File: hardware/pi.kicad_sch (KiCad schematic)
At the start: 4 parts, among them U1 RP2040, U2 W25Q128JVSIQ, U3 TJA1042T_3_1J, U4 105450-0101

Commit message: work on pi schematic
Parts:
- added C1, C2: 27p, jlc_footprints:C0402, symbol jlc:C0402C0G270G500NTB
- added C10, C11, C12, C13, C14, C5, C6, C7, C8, C9: 100nF, jlc_footprints:C0402, symbol jlc:CC0402KRX7R8BB104
- added C3, C4: 1uF, jlc_footprints:C0402, symbol jlc:0402X105K160
- added R1, R2: 5K1, jlc_footprints:R0402, symbol jlc:CR-02FL6---5K1
- added R3: 1K, jlc_footprints:R0402, symbol jlc:CR-02FL6----1K
- added R4, R5: 27R4, jlc_footprints:R0402, symbol jlc:WR04X27R4FTL
- added U5: NCP1117ST33T3G, jlc_footprints:SOT-223-3_L6.5-W3.4-P2.30-LS7.0-BR, symbol jlc:NCP1117ST33T3G
- added U6: SS54_C22452, jlc_footprints:SMA_L4.4-W2.8-LS5.4-R-RD, symbol jlc:SS54_C22452
- added U7: DS1129-05-S80BP-X, jlc_footprints:RJ45-TH_DS1129-05-S80BP-X, symbol jlc:DS1129-05-S80BP-X
- added X1: 12MHz, jlc_footprints:OSC-SMD_2P-L5.0-W3.2, symbol jlc:ABM3-12_000MHZ-D2Y-T
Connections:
- net USBC.GND is gone; now on net GND: U4.A1 (GND), U4.A12 (GND), U4.B1 (GND), U4.B12 (GND)
- net USBC.DM: now also R5.2; no longer U1.46 (USB_DM)
- net USBC.DP: now also R4.2; no longer U1.47 (USB_DP)
- net USBC.VBUS: now also U6.1 (A)
- net at U4.A5 (CC1): now also R2.1
- net at U4.B5 (CC2): now also R1.1
- net +3.3V: now reaches U1.1 (IOVDD)
- net +3.3V: now also U1.10 (IOVDD), U1.22 (IOVDD), U1.33 (IOVDD), U1.42 (IOVDD), U1.43 (ADC_AVDD), U1.44 (VREG_IN), U1.48 (USB_VDD), U1.49 (IOVDD), C10.1, C11.1, C12.1, C13.1, C14.1, C4.1, C7.1, C8.1, C9.1
- net GND: now reaches U1.19 (TESTEN)
- net GND: now also U1.57 (GND), C1.1, C10.2, C11.2, C12.2, C13.2, C14.2, C2.1, C3.2, C4.2, C5.2, C6.2, C7.2, C8.2, C9.2, R1.2, R2.2
- net at U1.20 (XIN): now also C1.2, X1.1 (OSC1)
- net at U1.21 (XOUT): now also R3.2
- net +1V1: now reaches U1.23 (DVDD)
- net +1V1: now also U1.45 (VREG_VOUT), U1.50 (DVDD), C3.1, C5.1, C6.1
- new net: R4.1, U1.47 (USB_DP)
- new net: R5.1, U1.46 (USB_DM)
- new net: C2.2, R3.1, X1.2 (OSC2)
- new net +5V: U6.2 (K)
- no-connect marks 0 -> 10
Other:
- title: (none) -> Pi RP2040 MCU
- moved on the sheet: U1, U2, U3, U4

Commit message: continue work on pi part
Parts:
- added C15, C18: 100nF, jlc_footprints:C0402, symbol jlc:CC0402KRX7R8BB104
- added C16, C17: 10uF, jlc_footprints:C0603, symbol jlc:TCC0603X5R106M100CT
- added C19: 4.7nF, jlc_footprints:C0402, symbol jlc:0402B472K500CT
- added C20, C21: 100pF, jlc_footprints:C0402, symbol jlc:CC0402JRNPO9BN101
- added C22: 47nF, jlc_footprints:C0402, symbol jlc:GCM155R71H473KE02J
- added H1: WS2812, jlc_footprints:HDR-TH_3P-P2.54-V-F, symbol jlc:22025403P00CKMT
- added H2: Debug, jlc_footprints:HDR-TH_6P-P2.54-V-F, symbol jlc:Header-Female-2_54_1x6
- added H3: T_CH, jlc_footprints:HDR-TH_2P-P2.54-V-M-1, symbol jlc:22-28-4020
- added H4: T_CL, jlc_footprints:HDR-TH_2P-P2.54-V-M-1, symbol jlc:22-28-4020
- added R10: 1M, jlc_footprints:R0402, symbol jlc:AC0402FR-071ML
- added R11, R12: 60R4, jlc_footprints:R1206, symbol jlc:AC1206FR-0760R4L
- added R6, R9: 1K, jlc_footprints:R0402, symbol jlc:CR-02FL6----1K
- added R7, R8: 10K, jlc_footprints:R0402, symbol jlc:CR-02FL6---10K
- added SW1: BOOTSEL, jlc_footprints:SW-SMD_L6.1-W3.6-LS6.6, symbol jlc:TS-1092U-B3D2
- added SW2: RESET, jlc_footprints:SW-SMD_L6.1-W3.6-LS6.6, symbol jlc:TS-1092U-B3D2
- added U8: WS2812E-V5, jlc_footprints:LED-SMD_4P-L5.0-W5.0-LS5.4-TL-1, symbol jlc:WS2812E-V5
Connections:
- net +3.3V: now also U2.8 (VCC), U3.5 (VIO), U5.2 (OUTPUT), U5.4 (TAB), C15.1, C17.1, C18.2, H2.1, R7.1, R8.2
- net +5V: now also U3.3 (VCC), U5.3 (INPUT), C16.1, C18.1, C22.1, H1.3, U8.1 (VDD)
- net GND: now also U2.4 (GND), U3.2 (GND), U3.8 (STB), U5.1 (ADJ/GND), C15.2, C16.2, C17.2, C19.2, C20.2, C21.1, C22.2, H1.1, H2.2, R10.2, SW1.2, SW2.2, U8.3 (GND)
- net SPI_FLASH.SS: now also R6.2, R7.2
- net at U7.17: now also U7.18, U7.19
- net USBC.SHIELD: now reaches U4.0 (25)
- net USBC.SHIELD: now also R10.1
- net at U3.1 (TXD): now also U1.36 (GPIO24)
- net at U3.4 (RXD): now also U1.37 (GPIO25)
- net at U3.6 (CANL): now also C21.2, H4.2
- net at U3.7 (CANH): now also C20.1, H3.2
- net IO8: now reaches U1.11 (GPIO8)
- net IO9: now reaches U1.12 (GPIO9)
- net IO10: now reaches U1.13 (GPIO10)
- net IO11: now reaches U1.14 (GPIO11)
- net I2C_SDA: now reaches U1.17 (GPIO14)
- net I2C_SCL: now reaches U1.18 (GPIO15)
- net IO0: now reaches U1.2 (GPIO0)
- net Debug_Clock: now reaches U1.24 (SWCLK)
- net Debug_Clock: now also H2.3
- net Debug_Data: now reaches U1.25 (SWD)
- net Debug_Data: now also H2.4
- net at U1.26 (RUN): now also R8.1, R9.1
- net Debug_Tx: now reaches U1.27 (GPIO16)
- net Debug_Tx: now also H2.5
- net Debug_Rx: now reaches U1.28 (GPIO17)
- net Debug_Rx: now also H2.6
- net IO1: now reaches U1.3 (GPIO1)
- net LED_Din: now reaches U1.35 (GPIO23)
- net LED_Din: now also U8.4 (DIN)
- net ADC0: now reaches U1.38 (GPIO26_ADC0)
- net ADC1: now reaches U1.39 (GPIO27_ADC1)
- net IO2: now reaches U1.4 (GPIO2)
- net ADC2: now reaches U1.40 (GPIO28_ADC2)
- net ADC3: now reaches U1.41 (GPIO29_ADC3)
- net IO3: now reaches U1.5 (GPIO3)
- net IO4: now reaches U1.6 (GPIO4)
- net IO5: now reaches U1.7 (GPIO5)
- net IO6: now reaches U1.8 (GPIO6)
- net IO7: now reaches U1.9 (GPIO7)
- new net: C19.1, R11.2, R12.1
- new net: H4.1, R12.2
- new net: H1.2, U8.2 (DO)
- new net: H3.1, R11.1
- new net: R9.2, SW2.1
- new net: R6.1, SW1.1
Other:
- note added: "3.3V Power Supply"
- note added: "CAN Transceiver"
- note added: "Debugging Connector"
- note added: "Status LED"
- moved on the sheet: U2, U3, U5, U7A, U7B

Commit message: more work on pi schematic
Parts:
- added C23: 100nF, jlc_footprints:C0402, symbol jlc:CC0402KRX7R8BB104
- added C24: 100uF, jlc_footprints:CAP-SMD_BD10.0-L10.3-W10.3-FD, symbol jlc:VZH101M1K1010-TRO
- added C25: 1000uF, jlc_footprints:CAP-SMD_BD10.0-L10.3-W10.3-LS11.3-FD, symbol jlc:VT1C102M1010
- added D1: MBR340F, jlc_footprints:SOD-123_L2.8-W1.8-LS3.7-RD, symbol jlc:MBR340F
- added H5: PWR, jlc_footprints:HDR-TH_2P-P2.54-V-M-1, symbol jlc:22-28-4020
- added R13, R14, R15, R16: 10K, jlc_footprints:R0402, symbol jlc:CR-02FL6---10K
- added R17: 1M, jlc_footprints:R0402, symbol jlc:AC0402FR-071ML
- added U10: SKCR-16S, jlc_footprints:SW-SMD_SM_SKCR-16S, symbol jlc:SKCR-16S
- added U11: LM2576S-5_0_TR, jlc_footprints:TO-263-5_L10.6-W9.6-P1.70-LS15.9-BR, symbol jlc:LM2576S-5_0_TR
- added U12: SS54_C22452, jlc_footprints:SMA_L4.4-W2.8-LS5.4-R-RD, symbol jlc:SS54_C22452
- added U13: 100uH, jlc_footprints:IND-SMD_L11.5-W10.0_YSPI1050, symbol jlc:YSPI1050-101M
- added U9: 74HC165D,653, jlc_footprints:SOIC-16_L9.9-W3.9-P1.27-LS6.0-BL, symbol jlc:74HC165D,653
- U7: value DS1129-05-S80BP-X -> CAN_IO
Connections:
- net +3.3V: now also C23.2, R13.1, R14.1, R15.1, R16.1, U9.16 (VCC)
- net +5V: now also U12.2 (K)
- net GND: now also U7.11, U7.14, U7.15, U7.3, U7.6, U7.7, C23.1, C24.2, C25.2, D1.2, R17.2, U10.C1 (C), U10.C2 (C), U11.3 (GND), U11.5 (ON#/OFF), U11.6 (TAB), U9.10 (DS), U9.15 (CE#), U9.8 (GND)
- net at C21.2, H4.2, U3.6 (CANL): now also U7.10, U7.2
- net at U7.1: now also C20.1, H3.2, U3.7 (CANH), U7.9
- net at U7.17, U7.18, U7.19: now also R17.1
- net at U7.4: now also U7.12, U7.13, U7.16, U7.5, U7.8, H5.1
- net IO12: now reaches U1.15 (GPIO12)
- net IO13: now reaches U1.16 (GPIO13)
- net IO14: now reaches U1.29 (GPIO18)
- net IO15: now reaches U1.30 (GPIO19)
- net SR_Load: now reaches U1.31 (GPIO20)
- net SR_Load: now also U9.1 (PL#)
- net SR_Clock: now reaches U1.32 (GPIO21)
- net SR_Clock: now also U9.2 (CP)
- net SR_Data: now reaches U1.34 (GPIO22)
- net SR_Data: now also U9.9 (Q7)
- new net: R13.2, U10.8, U9.6 (D7)
- new net: R15.2, U10.2, U9.4 (D5)
- new net: D1.1, U11.2 (OUT), U13.1
- new net: C25.1, U11.4 (FB), U12.1 (A), U13.2
- new net: R16.2, U10.1, U9.3 (D4)
- new net: R14.2, U10.4, U9.5 (D6)
- new net +VDC: C24.1, H5.2, U11.1 (VIN)
- new net HWID0: U9.11 (D0)
- new net HWID1: U9.12 (D1)
- new net HWID2: U9.13 (D2)
- new net HWID3: U9.14 (D3)
- no-connect marks 10 -> 11
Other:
- note added: "5V Power Supply"
- note added: "Hardware ID Pins"
- moved on the sheet: C16, C17, H1, H2, U5, U7A, U7B, U8

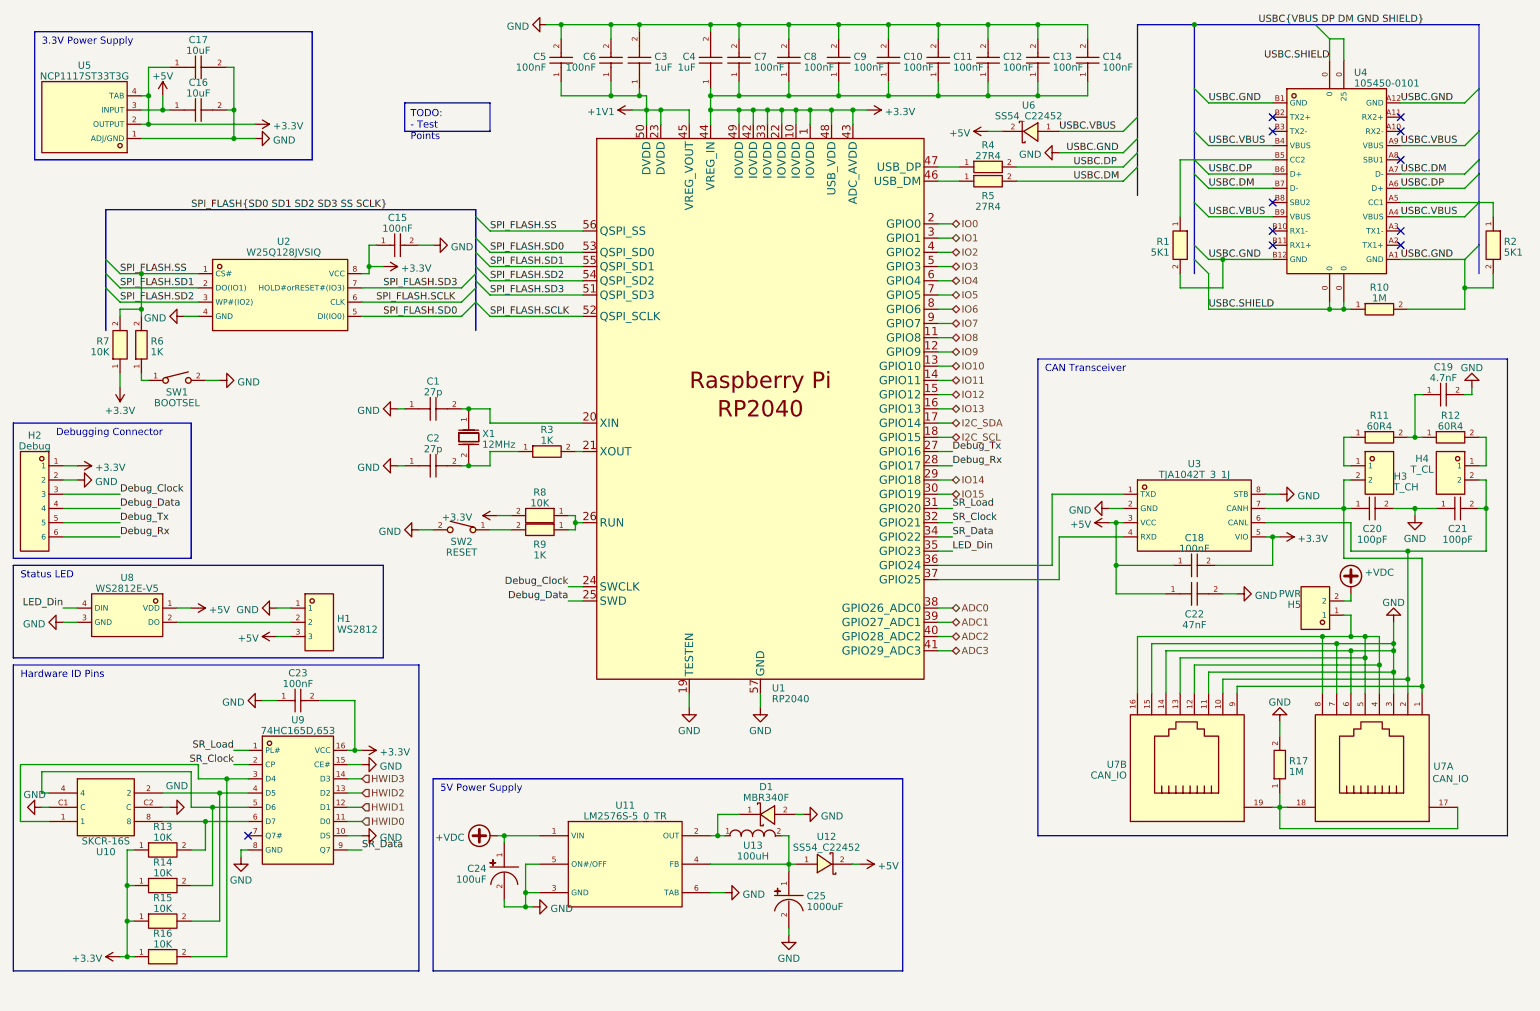
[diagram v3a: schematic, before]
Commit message: put lm2576 in own schematic sheet
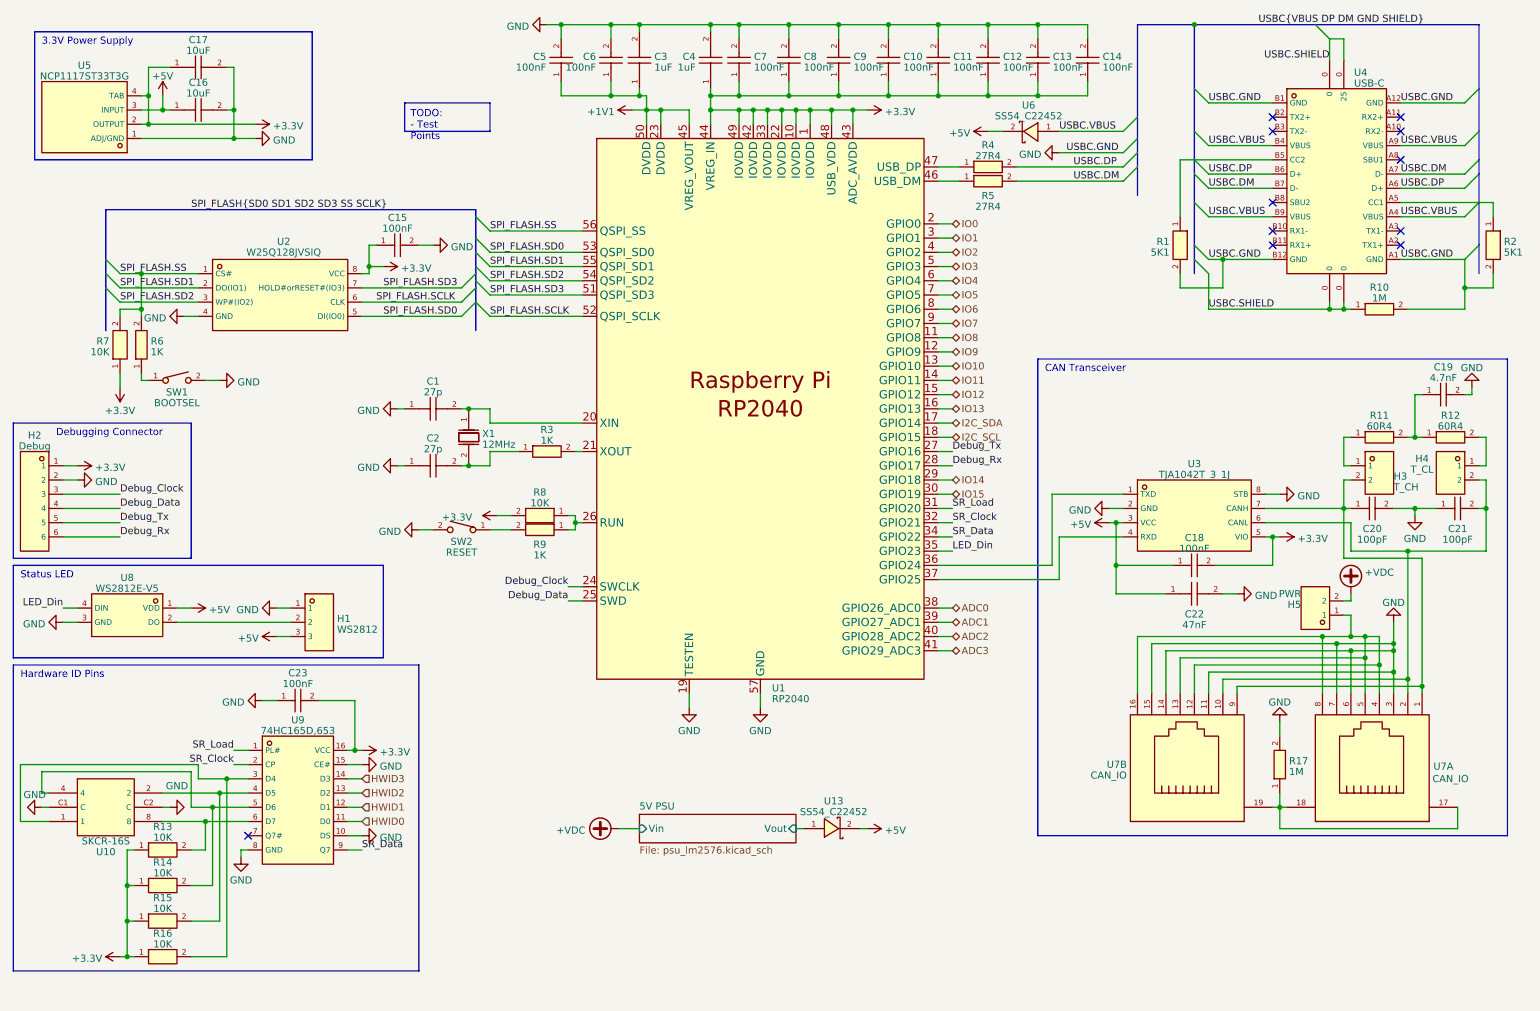
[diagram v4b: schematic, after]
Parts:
- removed C24: 100uF, jlc_footprints:CAP-SMD_BD10.0-L10.3-W10.3-FD, symbol jlc:VZH101M1K1010-TRO
- removed C25: 1000uF, jlc_footprints:CAP-SMD_BD10.0-L10.3-W10.3-LS11.3-FD, symbol jlc:VT1C102M1010
- removed D1: MBR340F, jlc_footprints:SOD-123_L2.8-W1.8-LS3.7-RD, symbol jlc:MBR340F
- removed U11: LM2576S-5_0_TR, jlc_footprints:TO-263-5_L10.6-W9.6-P1.70-LS15.9-BR, symbol jlc:LM2576S-5_0_TR
- removed U12: SS54_C22452, jlc_footprints:SMA_L4.4-W2.8-LS5.4-R-RD, symbol jlc:SS54_C22452
- removed U13: 100uH, jlc_footprints:IND-SMD_L11.5-W10.0_YSPI1050, symbol jlc:YSPI1050-101M
- added U13: SS54_C22452, jlc_footprints:SMA_L4.4-W2.8-LS5.4-R-RD, symbol jlc:SS54_C22452
- U4: value 105450-0101 -> USB-C
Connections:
- net +5V: now also U13.2 (K)
- new net 5V PSU/Vout: U13.1 (A)
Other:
- added sheet 5V PSU (psu_lm2576.kicad_sch)
- note removed: "5V Power Supply"

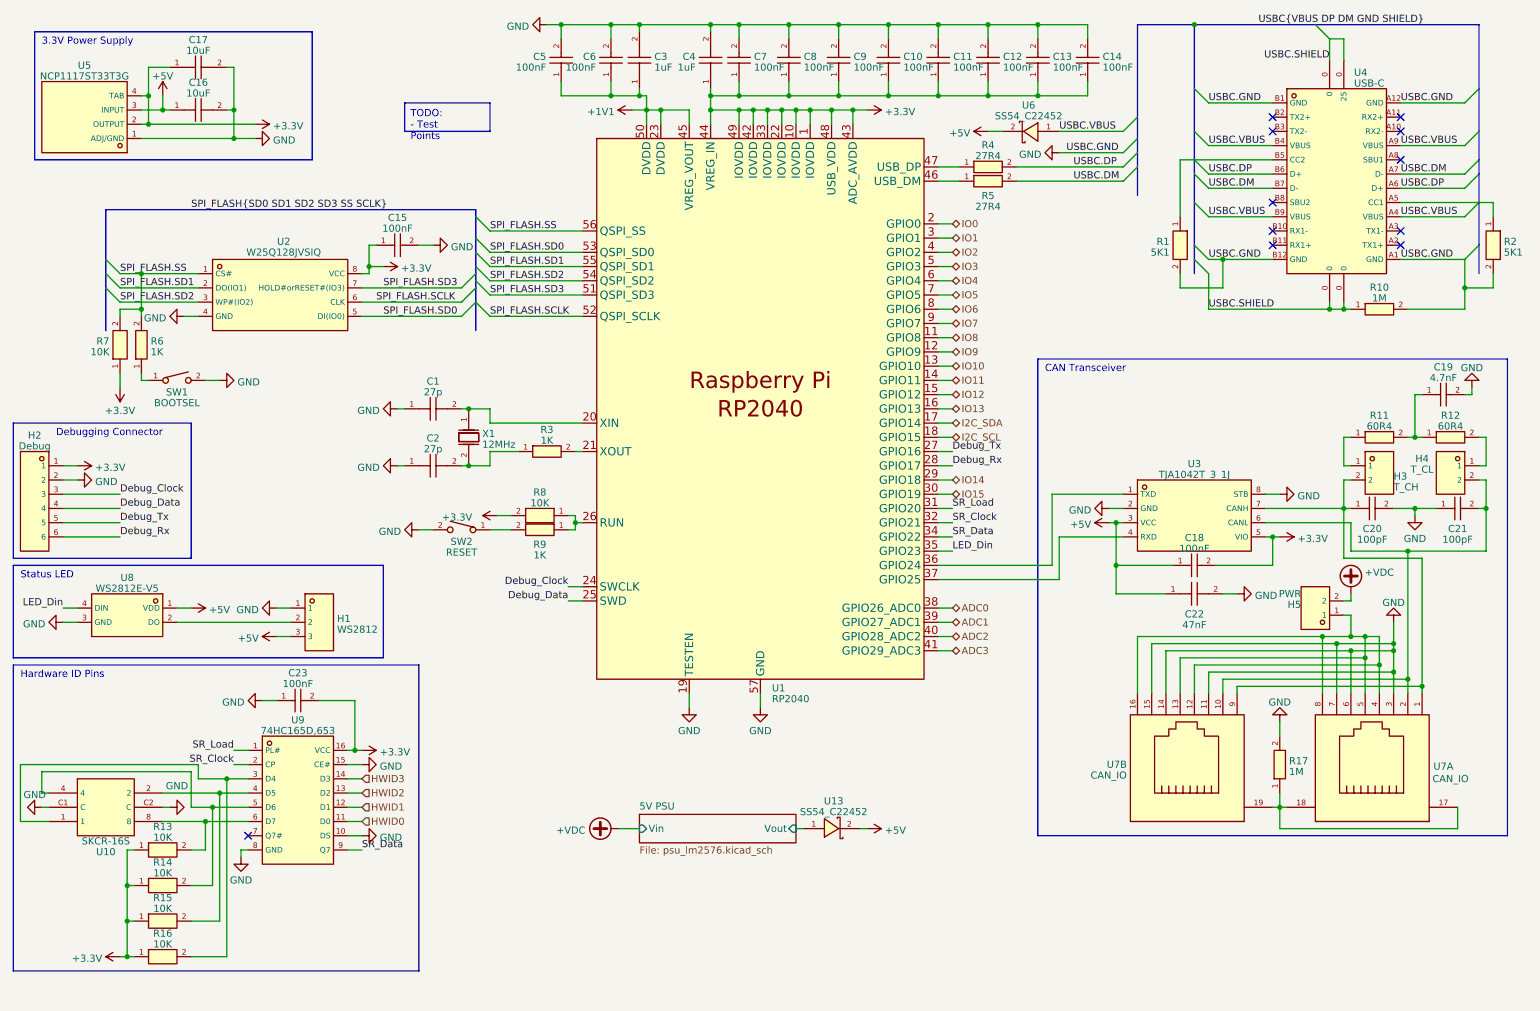
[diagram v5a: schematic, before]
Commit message: start working on mainboard pcb layout
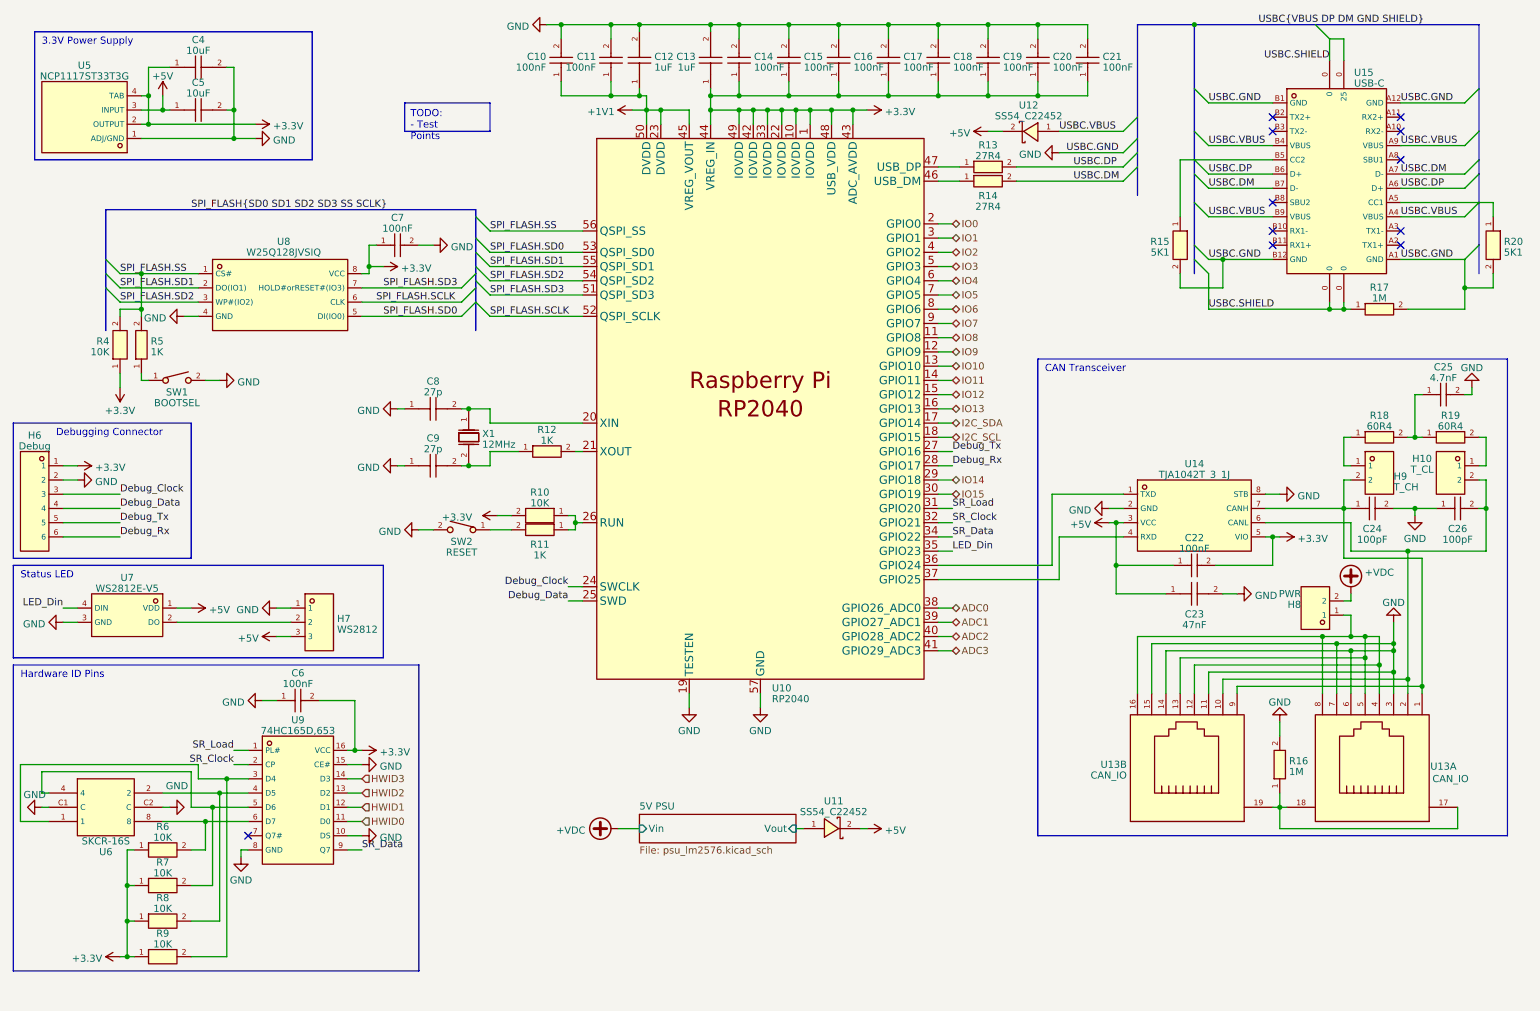
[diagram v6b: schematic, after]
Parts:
- renumbered C5 to C10, C6 to C11, C3 to C12, C4 to C13, C7 to C14, C8 to C15, C9 to C16, C10 to C17, C11 to C18, C12 to C19, C13 to C20, C14 to C21, C18 to C22, C22 to C23, C20 to C24, C19 to C25, C21 to C26, C17 to C4, C16 to C5, C23 to C6, C15 to C7, C1 to C8, C2 to C9, H4 to H10, H2 to H6, H1 to H7, H5 to H8, H3 to H9, R8 to R10, R9 to R11, R3 to R12, R4 to R13, R5 to R14, R1 to R15, R17 to R16, R10 to R17, R11 to R18, R12 to R19, R2 to R20, R7 to R4, R6 to R5, R13 to R6, R14 to R7, R15 to R8, R16 to R9, U1 to U10, U13 to U11, U6 to U12, U7 to U13, U3 to U14, U4 to U15, U10 to U6, U8 to U7, U2 to U8
